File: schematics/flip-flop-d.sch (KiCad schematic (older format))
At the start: 0 parts

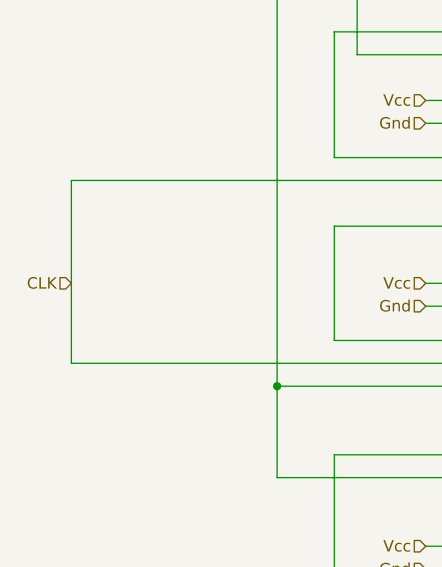
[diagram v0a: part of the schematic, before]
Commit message: Fleshes out basic schematics and some utility software
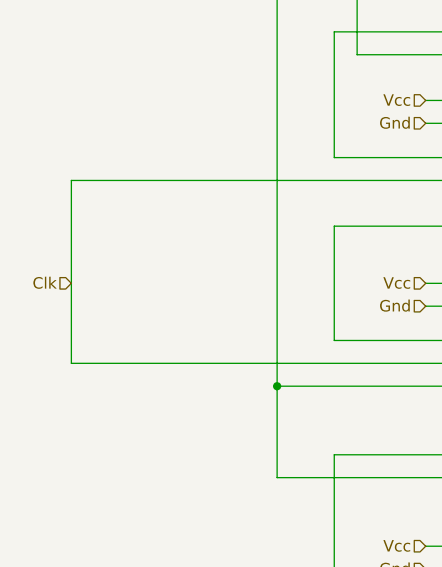
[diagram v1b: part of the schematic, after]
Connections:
- net labels added: Clk
- net labels removed: CLK
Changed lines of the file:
@@
 EESchema Schematic File Version 4
-LIBS:flip-flop-d-test-cache
 EELAYER 26 0
 EELAYER END
 $Descr A4 11693 8268
 encoding utf-8
-Sheet 2 9
+Sheet 2 16
 Title ""
 Date ""
@@
 D
 Text HLabel 1350 4050 0    50   Input ~ 0
-CLK
+Clk
 Wire Wire Line
 	3100 5550 1350 5550
